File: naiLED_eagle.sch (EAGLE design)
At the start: 8 parts, among them IC1 TCS3414, U2 24LC00T-I/OT, U3 ATTINY25-20SSU

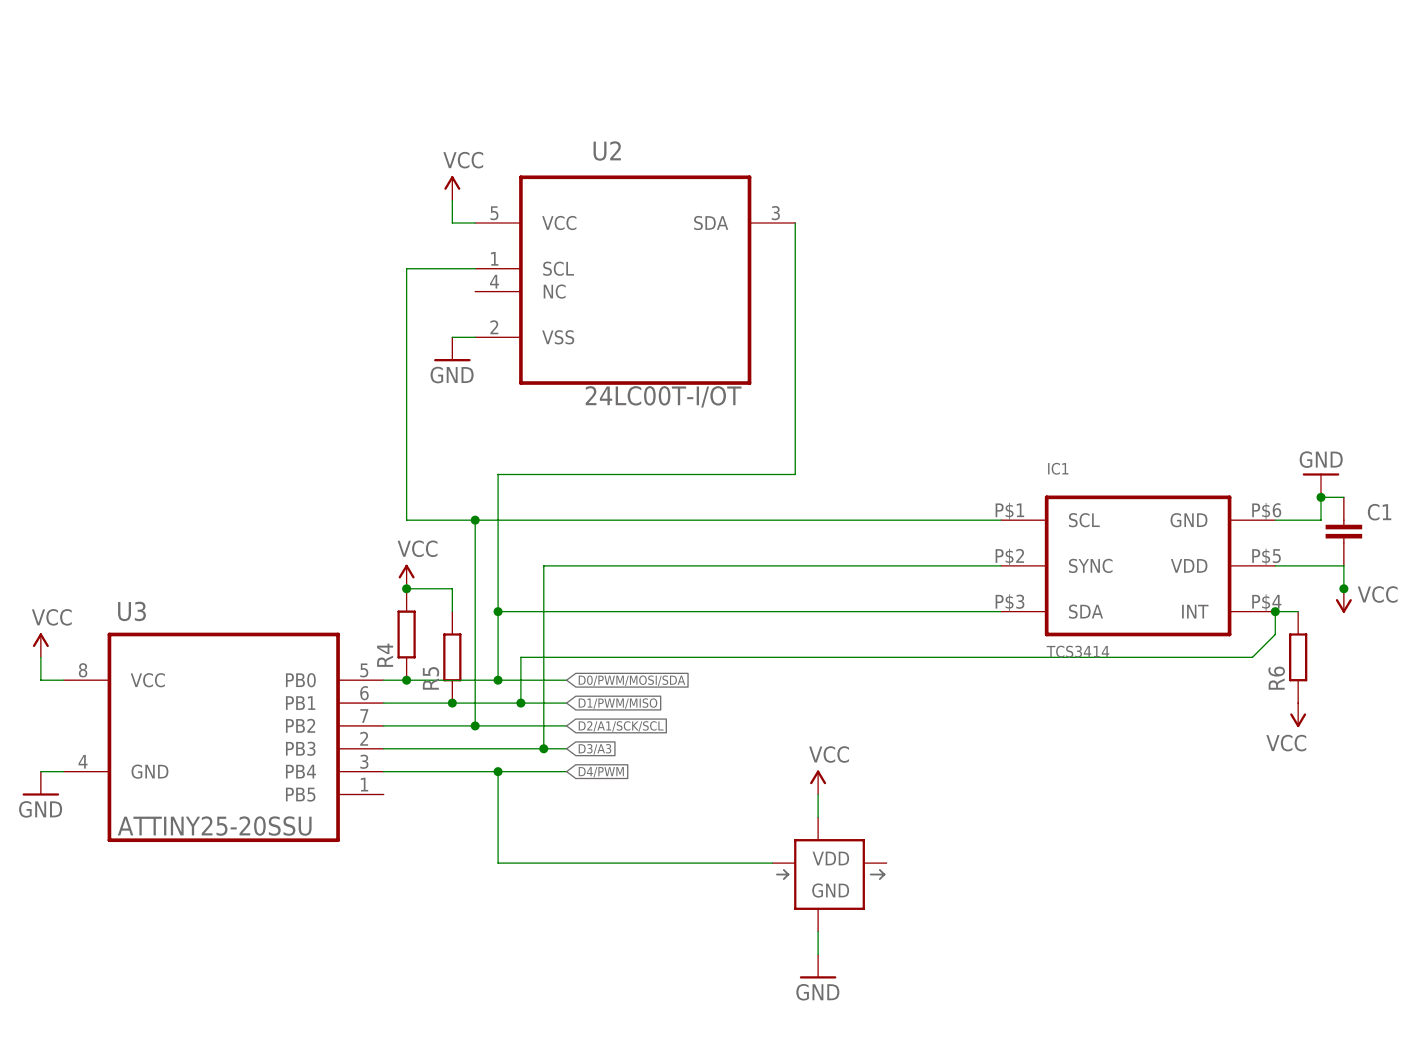
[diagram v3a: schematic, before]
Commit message: ripup all, added vias to attiny
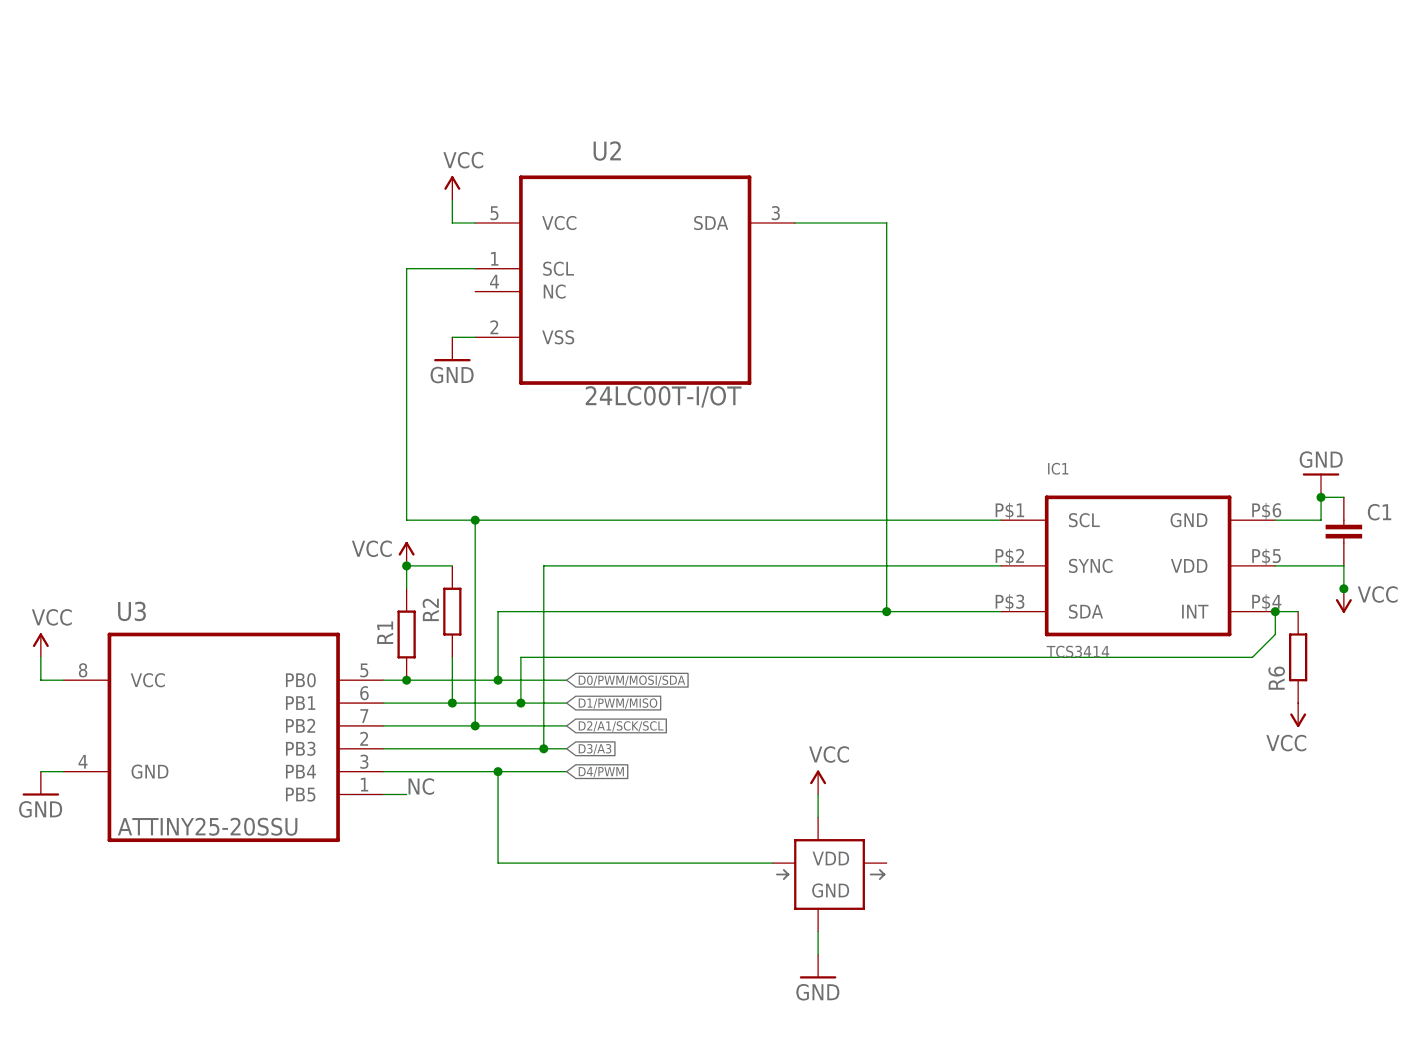
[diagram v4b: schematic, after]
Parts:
- removed R5: (no value), dp_devices:RESISTOR-0402
- added R2: (no value), dp_devices:RESISTOR-0402
- renumbered R4 to R1
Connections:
- new net NC: U3.PB5
- net D1/PWM/MISO: now also R2.1; no longer R5.1
- net VCC: now also R2.2; no longer R5.2
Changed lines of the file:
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@@
 <part name="P+4" library="SparkFun" deviceset="VCC" device=""/>
 <part name="P+3" library="SparkFun" deviceset="VCC" device=""/>
-<part name="R4" library="dp_devices" deviceset="RESISTOR" device="-0402"/>
-<part name="R5" library="dp_devices" deviceset="RESISTOR" device="-0402"/>
+<part name="R1" library="dp_devices" deviceset="RESISTOR" device="-0402"/>
+<part name="R2" library="dp_devices" deviceset="RESISTOR" device="-0402"/>
 <part name="P+5" library="SparkFun" deviceset="VCC" device=""/>
 <part name="R6" library="dp_devices" deviceset="RESISTOR" device="-0402"/>
@@
 <instance part="U3" gate="A" x="0" y="27.94" smashed="yes">
 <attribute name="NAME" x="-11.9634" y="37.084" size="2.0828" layer="95" ratio="10" rot="SR0"/>
-<attribute name="VALUE" x="-11.7856" y="13.2334" size="2.0828" layer="96" ratio="10" rot="SR0"/>
+<attribute name="VALUE" x="-11.7856" y="13.2334" size="1.9304" layer="96" ratio="10" rot="SR0"/>
 </instance>
 <instance part="GND1" gate="1" x="66.04" y="-2.54"/>
@@
 <attribute name="VALUE" x="125.984" y="39.116" size="1.778" layer="96"/>
 </instance>
-<instance part="P+3" gate="1" x="20.32" y="40.64"/>
-<instance part="R4" gate="G$1" x="20.32" y="35.56" rot="R90"/>
-<instance part="R5" gate="G$1" x="25.4" y="33.02" rot="R90"/>
+<instance part="P+3" gate="1" x="20.32" y="43.18" smashed="yes">
+<attribute name="VALUE" x="14.224" y="44.196" size="1.778" layer="96"/>
+</instance>
+<instance part="R1" gate="G$1" x="20.32" y="35.56" smashed="yes" rot="R90">
+<attribute name="NAME" x="18.8214" y="34.29" size="1.778" layer="95" font="vector" rot="R90"/>
+<attribute name="VALUE" x="23.622" y="31.75" size="1.778" layer="96" font="vector" rot="R90"/>
+</instance>
+<instance part="R2" gate="G$1" x="25.4" y="38.1" smashed="yes" rot="R90">
+<attribute name="NAME" x="23.9014" y="36.83" size="1.778" layer="95" font="vector" rot="R90"/>
+<attribute name="VALUE" x="28.702" y="34.29" size="1.778" layer="96" font="vector" rot="R90"/>
+</instance>
 <instance part="P+5" gate="1" x="119.38" y="27.94" rot="R180"/>
 <instance part="R6" gate="G$1" x="119.38" y="33.02" rot="R90"/>
@@
 </segment>
 <segment>
-<pinref part="R4" gate="G$1" pin="2"/>
+<pinref part="R1" gate="G$1" pin="2"/>
 <pinref part="P+3" gate="1" pin="VCC"/>
-<wire x1="20.32" y1="40.64" x2="25.4" y2="40.64" width="0.1524" layer="91"/>
-<junction x="20.32" y="40.64"/>
-<pinref part="R5" gate="G$1" pin="2"/>
-<wire x1="25.4" y1="40.64" x2="25.4" y2="38.1" width="0.1524" layer="91"/>
+<wire x1="20.32" y1="43.18" x2="25.4" y2="43.18" width="0.1524" layer="91"/>
+<junction x="20.32" y="43.18"/>
+<pinref part="R2" gate="G$1" pin="2"/>
+<wire x1="20.32" y1="43.18" x2="20.32" y2="40.64" width="0.1524" layer="91"/>
 </segment>
 <segment>
@@
 <segment>
 <pinref part="U3" gate="A" pin="PB1"/>
+<label x="38.1" y="27.94" size="1.016" layer="95" xref="yes"/>
 <wire x1="17.78" y1="27.94" x2="25.4" y2="27.94" width="0.1524" layer="91"/>
-<label x="38.1" y="27.94" size="1.016" layer="95" xref="yes"/>
 <wire x1="25.4" y1="27.94" x2="33.02" y2="27.94" width="0.1524" layer="91"/>
 <wire x1="33.02" y1="27.94" x2="38.1" y2="27.94" width="0.1524" layer="91"/>
-<pinref part="R5" gate="G$1" pin="1"/>
-<junction x="25.4" y="27.94"/>
 <pinref part="IC1" gate="A" pin="INT"/>
 <wire x1="116.84" y1="38.1" x2="119.38" y2="38.1" width="0.1524" layer="91"/>
@@
 <wire x1="33.02" y1="33.02" x2="33.02" y2="27.94" width="0.1524" layer="91"/>
 <junction x="33.02" y="27.94"/>
+<pinref part="R2" gate="G$1" pin="1"/>
+<wire x1="25.4" y1="33.02" x2="25.4" y2="27.94" width="0.1524" layer="91"/>
+<junction x="25.4" y="27.94"/>
 </segment>
 </net>
@@
 <segment>
 <pinref part="U2" gate="A" pin="SDA"/>
-<wire x1="63.5" y1="81.28" x2="63.5" y2="53.34" width="0.1524" layer="91"/>
-<wire x1="63.5" y1="53.34" x2="30.48" y2="53.34" width="0.1524" layer="91"/>
 <pinref part="U3" gate="A" pin="PB0"/>
 <wire x1="20.32" y1="30.48" x2="30.48" y2="30.48" width="0.1524" layer="91"/>
@@
 <pinref part="IC1" gate="A" pin="SDA"/>
 <wire x1="30.48" y1="30.48" x2="38.1" y2="30.48" width="0.1524" layer="91"/>
-<wire x1="86.36" y1="38.1" x2="30.48" y2="38.1" width="0.1524" layer="91"/>
+<wire x1="86.36" y1="38.1" x2="73.66" y2="38.1" width="0.1524" layer="91"/>
+<wire x1="73.66" y1="38.1" x2="30.48" y2="38.1" width="0.1524" layer="91"/>
 <wire x1="30.48" y1="38.1" x2="30.48" y2="30.48" width="0.1524" layer="91"/>
 <junction x="30.48" y="30.48"/>
-<wire x1="30.48" y1="53.34" x2="30.48" y2="38.1" width="0.1524" layer="91"/>
-<junction x="30.48" y="38.1"/>
-<pinref part="R4" gate="G$1" pin="1"/>
+<pinref part="R1" gate="G$1" pin="1"/>
 <junction x="20.32" y="30.48"/>
 <wire x1="20.32" y1="30.48" x2="17.78" y2="30.48" width="0.1524" layer="91"/>
+<wire x1="63.5" y1="81.28" x2="73.66" y2="81.28" width="0.1524" layer="91"/>
+<wire x1="73.66" y1="81.28" x2="73.66" y2="38.1" width="0.1524" layer="91"/>
+<junction x="73.66" y="38.1"/>
 </segment>
 </net>
@@
 </segment>
 </net>
+<net name="NC" class="0">
+<segment>
+<pinref part="U3" gate="A" pin="PB5"/>
+<wire x1="17.78" y1="17.78" x2="20.32" y2="17.78" width="0.1524" layer="91"/>
+<label x="20.32" y="17.78" size="1.778" layer="95"/>
+</segment>
+</net>

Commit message: mem docs
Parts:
- removed C1: (no value), dp_devices:CAPACITOR_NPOL-0402
- removed IC1: TCS3414, yair_r:TCS3414
- removed R6: (no value), dp_devices:RESISTOR-0402
- added C2: (no value), naiLED_eagle:CAPACITOR_NPOL-0402
- added U$2: VEML6040, naiLED_eagle:VEML6040
- R1, R2: device dp_devices:RESISTOR-0402 -> naiLED_eagle:RESISTOR-0402
- U$1: device pimoroni-optoelectronics:SK6812MINI -> naiLED_eagle:SK6812MINI
- U2: device Microchip-24LCxxx:24LC00T-I/OT -> naiLED_eagle:24LC00T-I/OT
- U3: value ATTINY25-20SSU -> ATTINY85-20SU; device yair_r:ATTINY25-20SSU -> naiLED_eagle:ATTINY85-20SU
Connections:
- net D0/PWM/MOSI/SDA: now also U$2.SDA; no longer IC1.SDA
- net D1/PWM/MISO: no longer IC1.INT, R2.1, R6.2
- net D2/A1/SCK/SCL: now also R2.1, U$2.SCL; no longer IC1.SCL
- net D3/A3: no longer IC1.SYNC
- net GND: now also C2.1, U$2.GND; no longer C1.2, IC1.GND
- net VCC: now also C2.2, U$2.VDD; no longer C1.1, IC1.VDD, R6.1
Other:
- moved on the sheet: U2

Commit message: new memory
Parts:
- removed U2: 24LC00T-I/OT, naiLED_eagle:24LC00T-I/OT
- added U1: AT24C256C-MAHL-T, naiLED_eagle:AT24C256C-MAHL-T
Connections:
- net D0/PWM/MOSI/SDA: now also U1.SDA; no longer U2.SDA
- net D2/A1/SCK/SCL: now also U1.SCL; no longer U2.SCL
- net GND: now also U1.A0, U1.A1, U1.A2, U1.GND; no longer U2.VSS
- net VCC: now also U1.VCC; no longer U2.VCC
